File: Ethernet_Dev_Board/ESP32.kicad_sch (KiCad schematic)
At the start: 19 parts, among them J401 TAG-CONNECT_NL_10-POS_LEGS, U401 74AUP1T08GWH, U402 ESP32-WROOM-32E

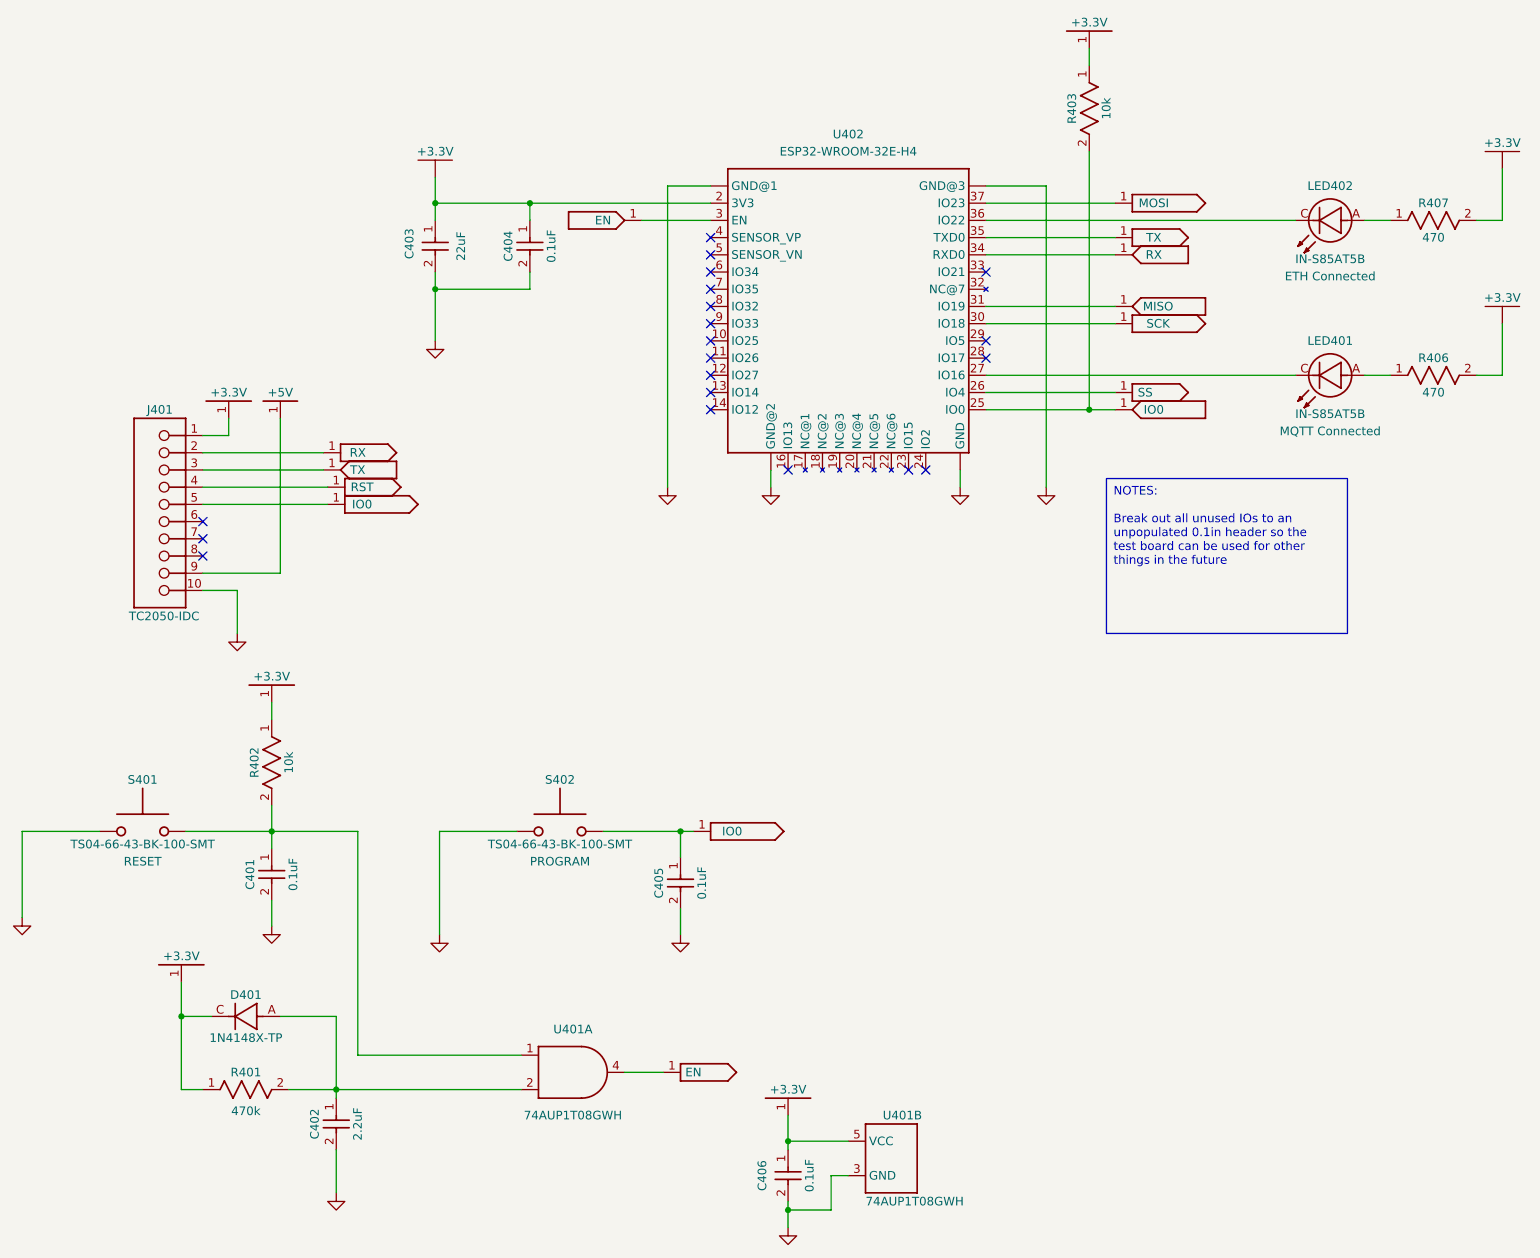
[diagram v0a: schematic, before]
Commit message: Added in 1.2 V regulator and broke out unused IO pins to header
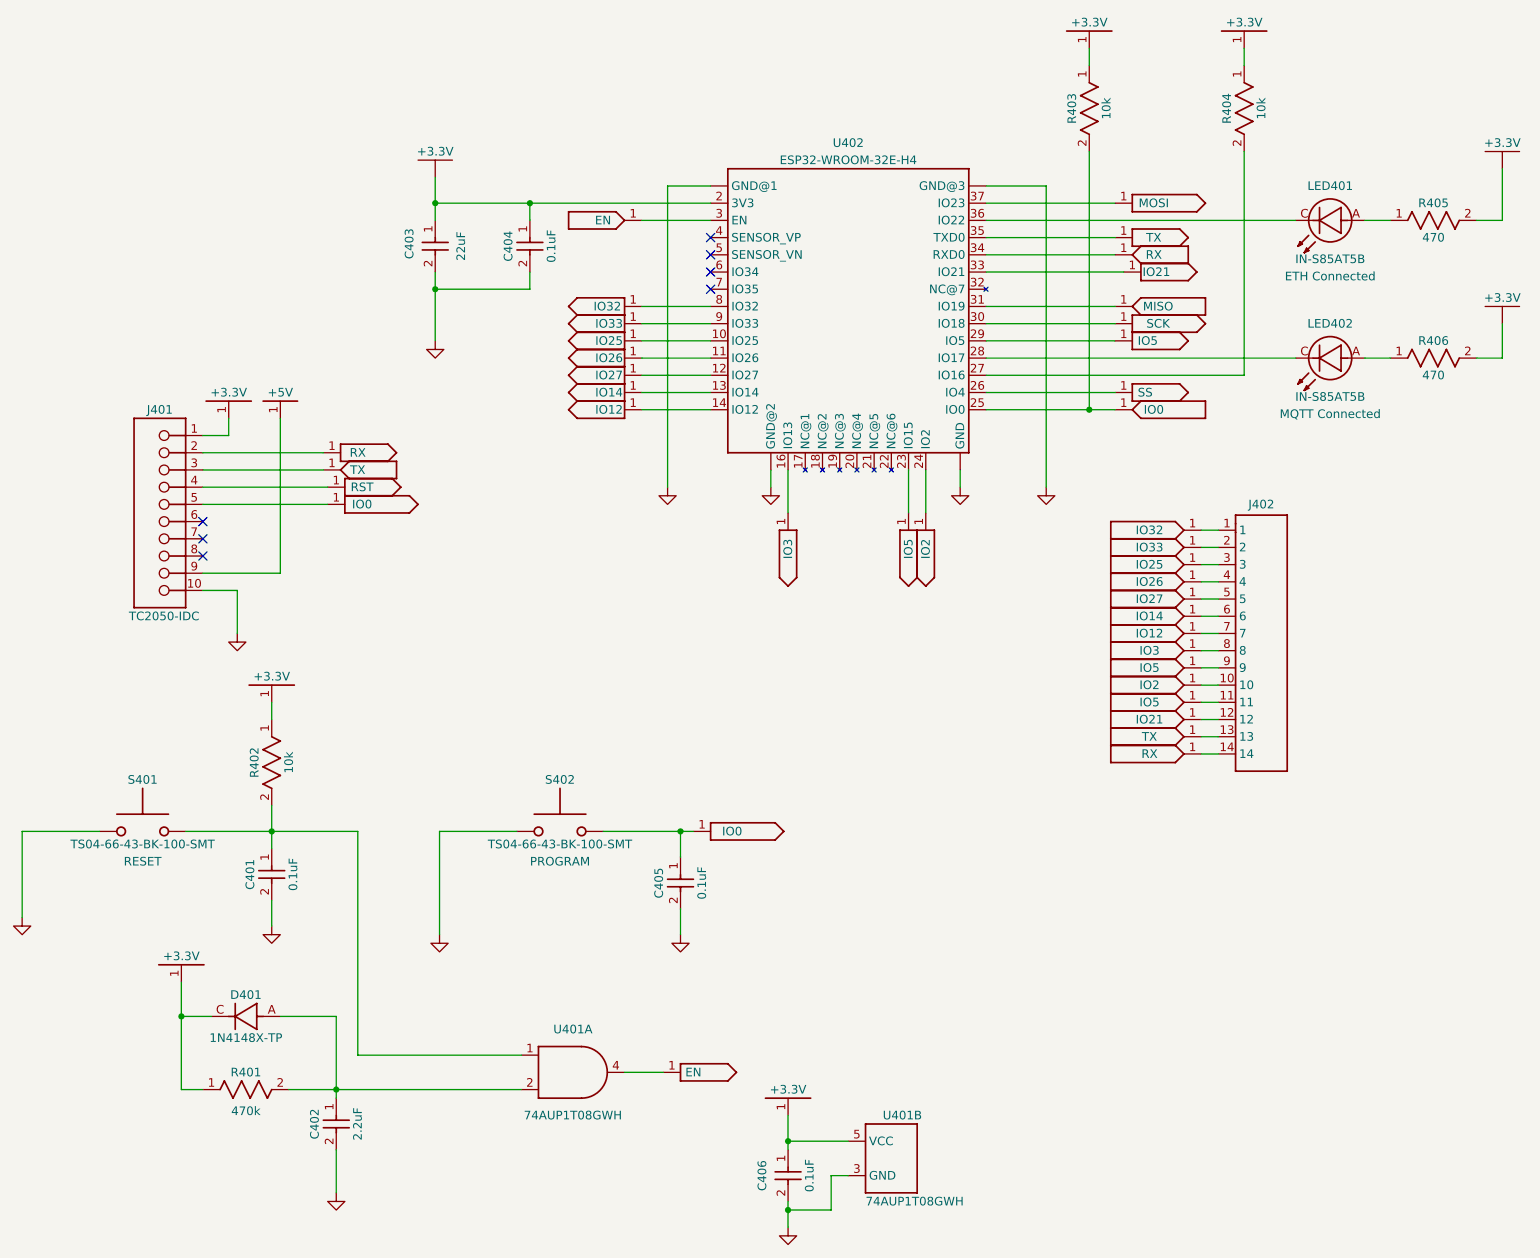
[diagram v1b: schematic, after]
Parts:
- added J402: ~, Connector_PinHeader_2.54mm:PinHeader_1x14_P2.54mm_Vertical, symbol RG_Connectors:Gen_Conn_1x14
- added R404: 10k, RG_Resistors_SMD:0603, symbol LED_Controller_Hardware-eagle-import:RES-0603
- renumbered LED402 to LED401, LED401 to LED402, R407 to R405
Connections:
- net +3.3V: now also R404.1
- net RX: now also J402.14
- net TX: now also J402.13
- net IO25: now reaches U402.10 (IO25)
- net IO25: now also J402.3
- net IO26: now reaches U402.11 (IO26)
- net IO26: now also J402.4
- net IO27: now reaches U402.12 (IO27)
- net IO27: now also J402.5
- net IO14: now reaches U402.13 (IO14)
- net IO14: now also J402.6
- net IO12: now reaches U402.14 (IO12)
- net IO12: now also J402.7
- net IO3: now reaches U402.16 (IO13)
- net IO3: now also J402.8
- net IO5: now reaches U402.23 (IO15)
- net IO5: now also U402.29 (IO5), J402.11, J402.9
- net IO2: now reaches U402.24 (IO2)
- net IO2: now also J402.10
- net at U402.27 (IO16): now also R404.2; no longer LED402.C
- net at U402.28 (IO17): now also LED402.C
- net IO21: now reaches U402.33 (IO21)
- net IO21: now also J402.12
- net IO32: now reaches U402.8 (IO32)
- net IO32: now also J402.1
- net IO33: now reaches U402.9 (IO33)
- net IO33: now also J402.2
- no-connect marks 20 -> 7
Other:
- moved on the sheet: LED402, R406

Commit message: Net adjustments. Beginning board layout
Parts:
- LED401: value ETH Connected -> ETH
- LED402: value MQTT Connected -> MQTT
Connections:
- net +3.3V: now also J402.1
- net IO12: now also J402.8; no longer J402.7
- net IO14: now also J402.7; no longer J402.6
- net IO2: now also J402.11; no longer J402.10
- net IO21: now also J402.13; no longer J402.12
- net IO25: now also J402.4; no longer J402.3
- net IO26: now also J402.5; no longer J402.4
- net IO27: now also J402.6; no longer J402.5
- net IO3: now also J402.9; no longer J402.8
- net IO32: now also J402.2; no longer J402.1
- net IO33: now also J402.3; no longer J402.2
- net IO5: now also J402.10, J402.12; no longer J402.11, J402.9
- net RX: no longer J402.14
- net TX: no longer J402.13
- net ESP_RST: now reaches C401.1, R402.2, S401.1 (2), S401.3 (2), U401.1 (A)
- net GNDS renamed GND1
- net GND1: now also J402.14; no longer U402.41 (GND@3), U402.45 (GND@2), U402.48 (GND@2)

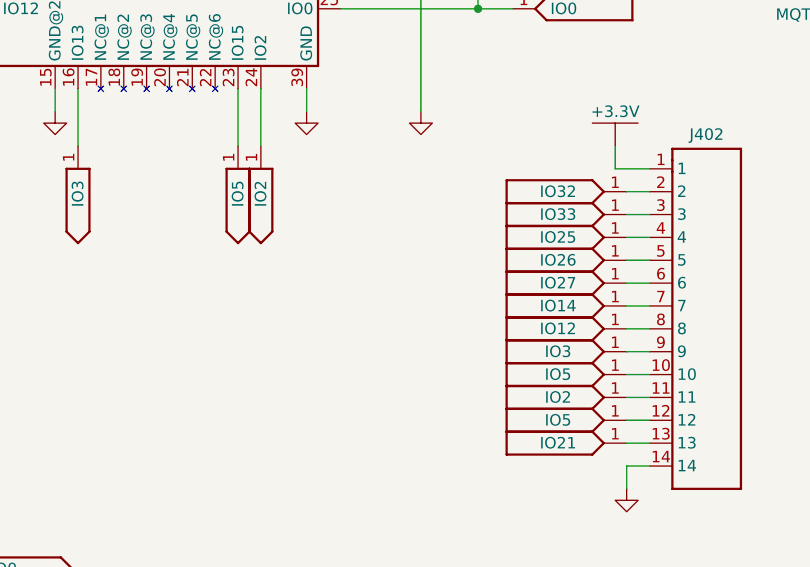
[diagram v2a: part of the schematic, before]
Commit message: Removed 1 TVS diode. removed 1 reset circuit. Placed Ethernet port in both W5500 and W5100S circuits
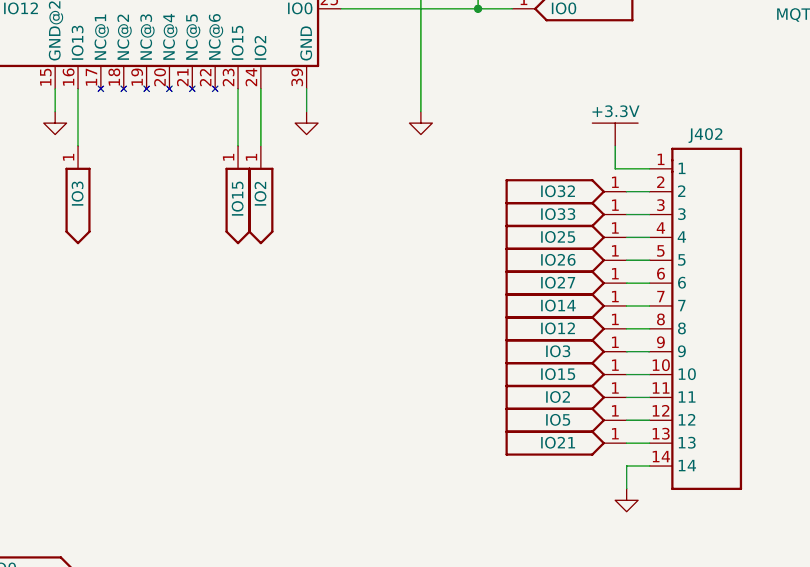
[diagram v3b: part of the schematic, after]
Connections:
- net IO5: no longer J402.10, U402.23 (IO15)
- new net IO15: J402.10, U402.23 (IO15)
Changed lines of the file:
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@@
 		(on_board yes)
 		(dnp no)
-		(property "Reference" "#NetPort0447"
+		(property "Reference" "#NetPort0445"
 			(at 210.82 19.05 0)
 			(effects
@@
 			(project "Ethernet_Dev_Board"
 				(path "/79118fbd-6cbf-48b1-af39-9f7b00f17642/7e416bb0-9118-4a80-b9f7-03742cbffb61"
-					(reference "#NetPort0447")
+					(reference "#NetPort0445")
 					(unit 1)
 				)
@@
 			)
 		)
-		(property "Value" "IO5"
+		(property "Value" "IO15"
 			(at 196.85 111.76 0)
 			(effects
@@
 			)
 		)
-		(property "Value" "IO5"
+		(property "Value" "IO15"
 			(at 161.29 90.17 0)
 			(effects
@@
 		(on_board yes)
 		(dnp no)
-		(property "Reference" "#PWR0415"
+		(property "Reference" "#PWR0417"
 			(at 248.92 62.23 0)
 			(effects
@@
 			(project "Ethernet_Dev_Board"
 				(path "/79118fbd-6cbf-48b1-af39-9f7b00f17642/7e416bb0-9118-4a80-b9f7-03742cbffb61"
-					(reference "#PWR0415")
+					(reference "#PWR0417")
 					(unit 1)
 				)
@@
 		(dnp no)
 		(fields_autoplaced yes)
-		(property "Reference" "#PWR0416"
+		(property "Reference" "#PWR0415"
 			(at 204.47 130.81 0)
 			(effects
@@
 			(project "Ethernet_Dev_Board"
 				(path "/79118fbd-6cbf-48b1-af39-9f7b00f17642/7e416bb0-9118-4a80-b9f7-03742cbffb61"
-					(reference "#PWR0416")
+					(reference "#PWR0415")
 					(unit 1)
 				)
@@
 		(on_board yes)
 		(dnp no)
-		(property "Reference" "#PWR0414"
+		(property "Reference" "#PWR0416"
 			(at 248.92 39.37 0)
 			(effects
@@
 			(project "Ethernet_Dev_Board"
 				(path "/79118fbd-6cbf-48b1-af39-9f7b00f17642/7e416bb0-9118-4a80-b9f7-03742cbffb61"
-					(reference "#PWR0414")
+					(reference "#PWR0416")
 					(unit 1)
 				)
@@
 		(on_board yes)
 		(dnp no)
-		(property "Reference" "#PWR0417"
+		(property "Reference" "#PWR0414"
 			(at 203.2 90.17 0)
 			(effects
@@
 			(project "Ethernet_Dev_Board"
 				(path "/79118fbd-6cbf-48b1-af39-9f7b00f17642/7e416bb0-9118-4a80-b9f7-03742cbffb61"
-					(reference "#PWR0417")
+					(reference "#PWR0414")
 					(unit 1)
 				)

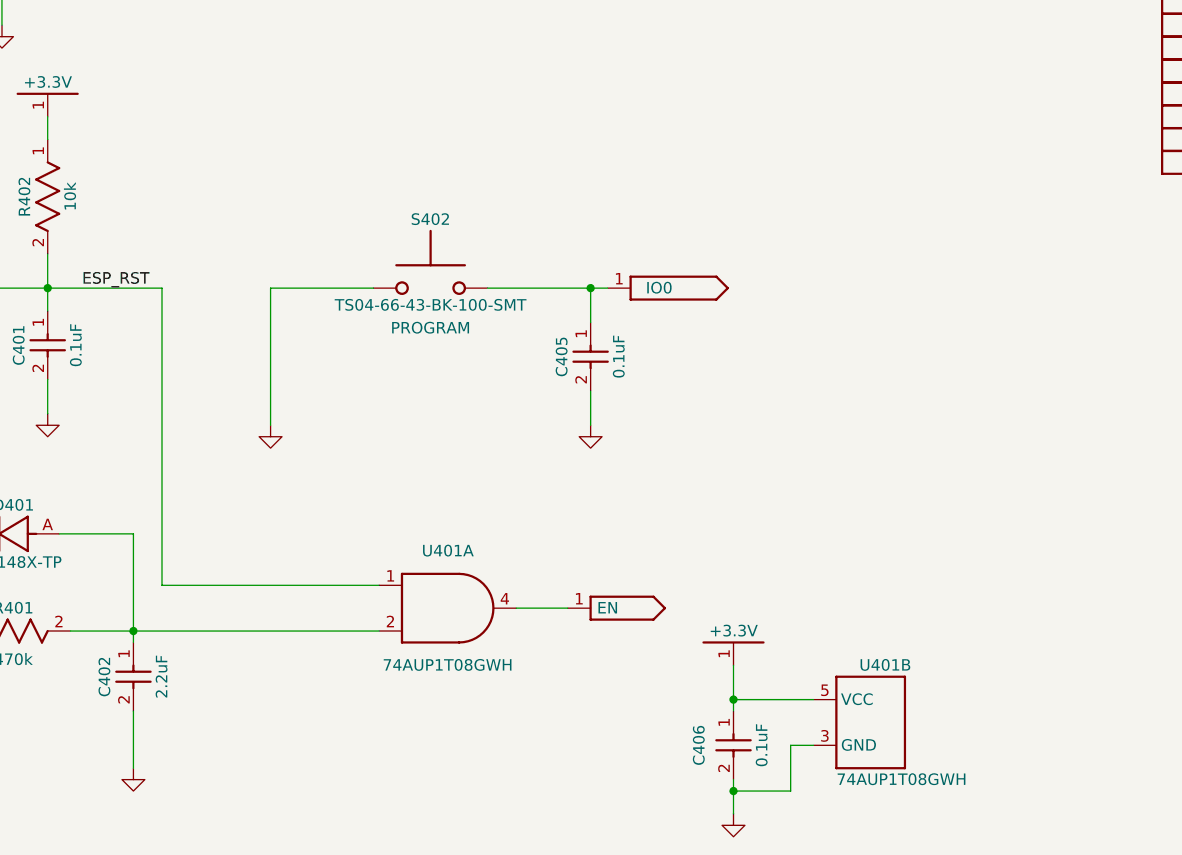
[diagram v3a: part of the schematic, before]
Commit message: Removed unnecessary nets. Beginning board routing
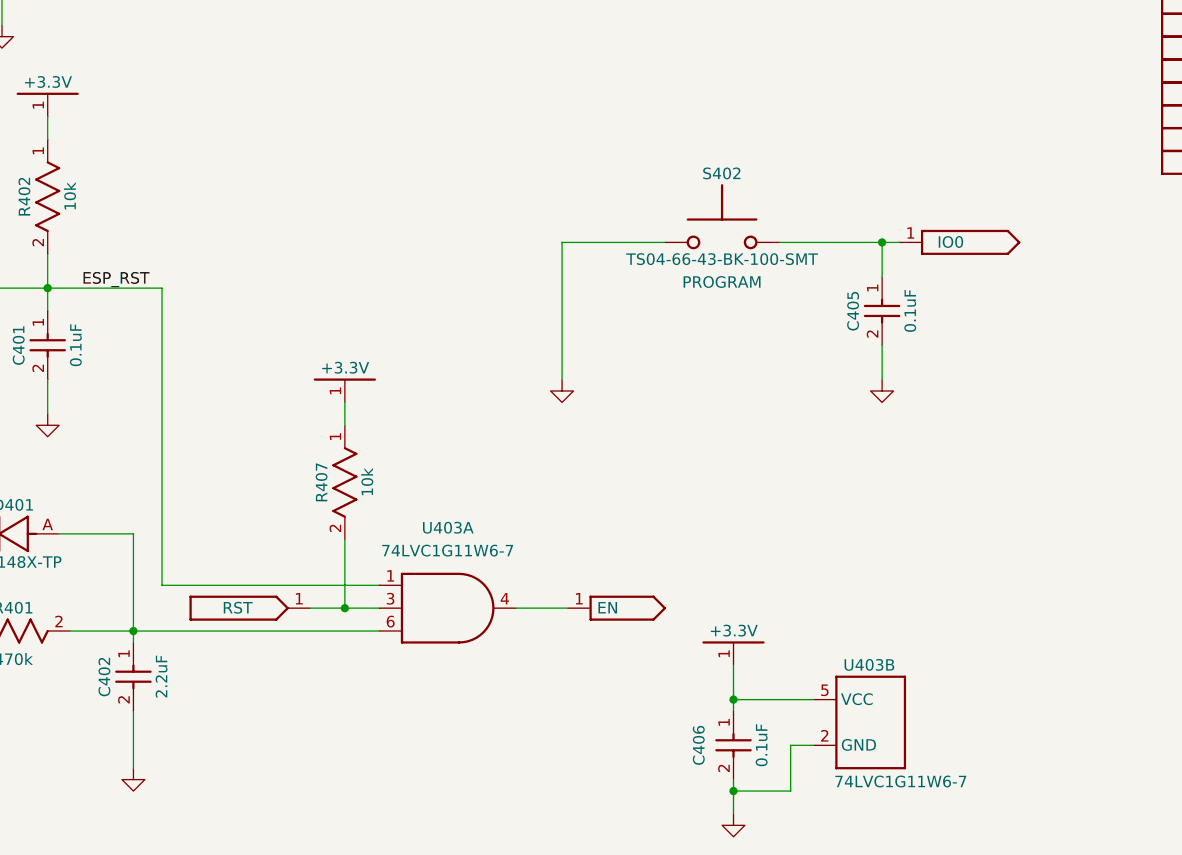
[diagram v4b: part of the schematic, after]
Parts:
- removed U401: 74AUP1T08GWH, RG_TO_SOT_SMD:SOT23-5P65, symbol RG_Logic:74AUP1T08GWH
- added R407: 10k, RG_Resistors_SMD:0603, symbol LED_Controller_Hardware-eagle-import:RES-0603
- added U403: 74LVC1G11W6, RG_TO_SOT_SMD:SOT23-6, symbol RG_Logic:74LVC1G11W6
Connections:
- net +3.3V: now also R407.1, U403.5 (VCC)
- net EN: now also U403.4 (Y)
- net ESP_RST: now also U403.1 (A)
- net GND1: now also U403.2 (GND)
- net RST: now also R407.2, U403.3 (B)
- net at C402.1, D401.A, R401.2: now also U403.6 (C)
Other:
- moved on the sheet: C405, S402
